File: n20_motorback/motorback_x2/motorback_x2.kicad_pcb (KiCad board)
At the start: 2 copper layers, 19.9 x 11 mm, 13 parts, among them J1 Servo wire input, J2 Conn_01x01_Male, J3 Conn_01x01_Male, J4 prog_pins, U1 DRV8837DSGR, U2 ATtiny4-TS, U3 AIC1734-33GUTR

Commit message: mechanical improvements
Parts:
- moved C1 7.83 mm to (159.2, 115.4), turned to 180 degrees
- moved C2 7.47 mm to (161.3, 115.6), turned to 90 degrees
- moved U1 7.12 mm to (164.0, 116.4), turned to 45 degrees
- moved U2 2.90 mm to (169.3, 116.6)
- moved R2 2.00 mm to (172.5, 116.8)
- moved C3 0.70 mm to (166.0, 119.7)
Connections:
- J4 pad 4: /MOTORF -> /MOTORR
- J4 pad 5: /MOTORR -> /MOTORF
- U2 pad 1: /MOTORR -> /MOTORF
- U2 pad 3: /MOTORF -> /MOTORR
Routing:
- net /MOTORF: track 23.6 -> 9.34 mm
- net VBAT: track 20.9 -> 33.1 mm, vias 0 -> 4
- net /MOTORR: track 21.5 -> 9.59 mm
- net /VLOGIC: track 32.0 -> 22.1 mm, vias 3 -> 1
- net /MOTOROUT1: track 2.90 -> 8.41 mm
- net /MOTOROUT2: track 7.38 -> 3.03 mm
- net GND: track 26.5 -> 29.8 mm, vias 8 -> 6
- net BLINKY: track 9.41 -> 11.7 mm
- net PWMIN: track 6.67 -> 8.11 mm
- net /PWMR: track 3.10 -> 2.20 mm
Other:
- outline, holes or cut-outs redrawn

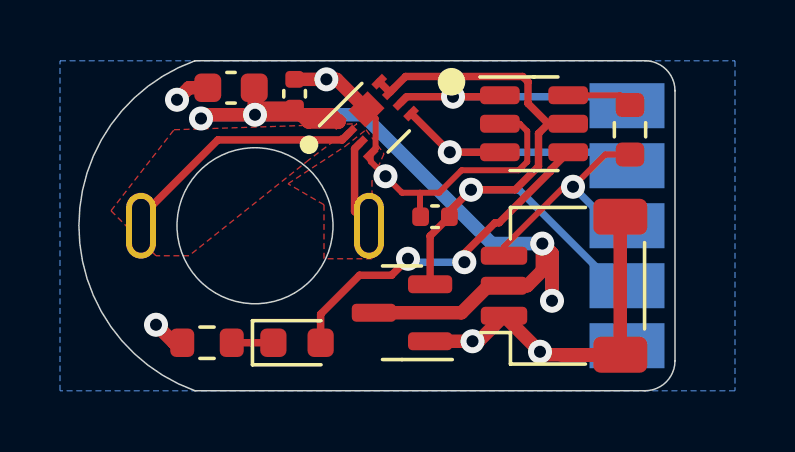
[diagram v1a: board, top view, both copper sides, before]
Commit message: Correct tpiclk / tpidata confusion
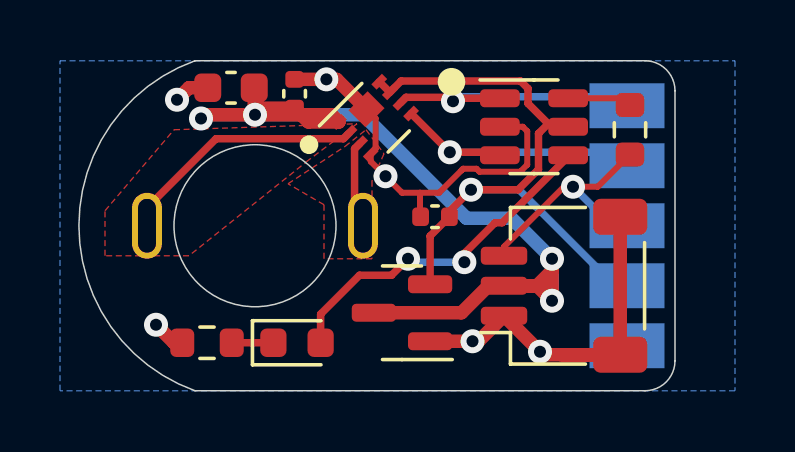
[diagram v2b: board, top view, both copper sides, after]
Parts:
- moved J2 0.20 mm to (156.6, 120.0)
- moved J3 0.20 mm to (163.4, 120.0)
- moved U2 0.10 mm to (169.3, 116.7)
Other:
- outline, holes or cut-outs redrawn

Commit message: minor fixups
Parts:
- moved U1 0.51 mm to (164.5, 116.5)
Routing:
- net /MOTOROUT1: track 8.39 -> 0.00 mm
- net /MOTOROUT2: track 2.95 -> 0.00 mm
- net /MOTORF: track 9.47 -> 8.93 mm
- net GND: track 29.9 -> 30.5 mm

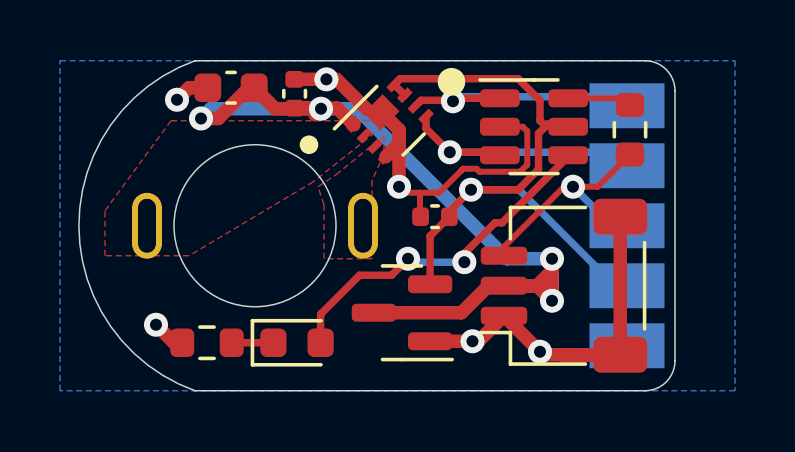
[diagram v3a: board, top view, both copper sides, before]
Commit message: Optional pull-down resistor
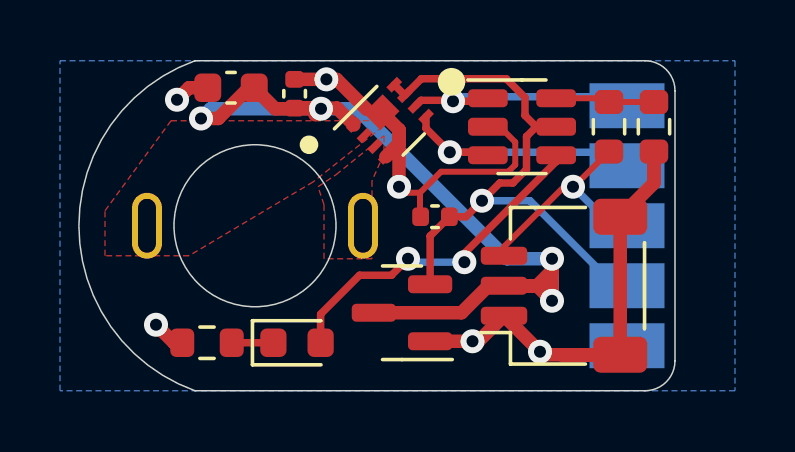
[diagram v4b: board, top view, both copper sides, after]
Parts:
- added R3: DNP, Resistor_SMD:R_0603_1608Metric, F.Cu at (173.3, 116.7)
- moved R2 0.71 mm to (171.8, 116.7)
- moved U2 0.40 mm to (168.9, 116.7)
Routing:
- net GND: track 30.5 -> 32.9 mm
- net /VLOGIC: track 21.8 -> 20.1 mm
- net /PWMR: track 2.16 -> 2.91 mm
- net PWMIN: track 8.11 -> 7.45 mm

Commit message: remove unnecessary bits
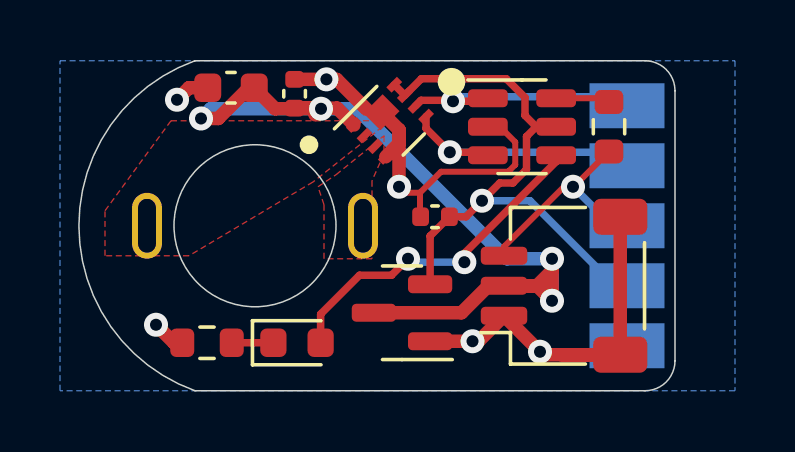
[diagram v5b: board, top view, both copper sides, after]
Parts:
- removed R3: DNP, Resistor_SMD:R_0603_1608Metric
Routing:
- net GND: track 32.9 -> 29.3 mm
- net /PWMR: track 2.91 -> 1.41 mm
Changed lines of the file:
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@@
-    )
-  )
-  (footprint "Resistor_SMD:R_0603_1608Metric" (layer "F.Cu")
-    (at 173.3 116.7 -90)
-    (descr "Resistor SMD 0603 (1608 Metric), square (rectangular) end terminal, IPC_7351 nominal, (Body size source: IPC-SM-782 page 72, https://www.pcb-3d.com/wordpress/wp-content/uploads/ipc-sm-782a_amendment_1_and_2.pdf), generated with kicad-footprint-generator")
-    (tags "resistor")
-    (property "LCSC" "")
-    (property "Sheet file" "motorback_x2.kicad_sch")
-    (property "Sheet name" "")
-    (attr smd)
-    (fp_text reference "R3" (at 0 -1.43 90) (layer "F.SilkS") hide
-      (effects (font (size 1 1) (thickness 0.15)))
-    )
-    (fp_text value "DNP" (at 0 1.43 90) (layer "F.Fab")
-      (effects (font (size 1 1) (thickness 0.15)))
-    )
-    (fp_text user "${REFERENCE}" (at 0 0 90) (layer "F.Fab")
-      (effects (font (size 0.4 0.4) (thickness 0.06)))
-    )
-    (fp_line (start -0.237258 0.5225) (end 0.237258 0.5225) (layer "F.SilkS") (width 0.12))
-    (fp_line (start -0.237258 -0.5225) (end 0.237258 -0.5225) (layer "F.SilkS") (width 0.12))
-    (fp_line (start -1.48 -0.73) (end 1.48 -0.73) (layer "F.CrtYd") (width 0.05))
-    (fp_line (start -1.48 0.73) (end -1.48 -0.73) (layer "F.CrtYd") (width 0.05))
-    (fp_line (start 1.48 0.73) (end -1.48 0.73) (layer "F.CrtYd") (width 0.05))
-    (fp_line (start 1.48 -0.73) (end 1.48 0.73) (layer "F.CrtYd") (width 0.05))
-    (fp_line (start -0.8 -0.4125) (end 0.8 -0.4125) (layer "F.Fab") (width 0.1))
-    (fp_line (start -0.8 0.4125) (end -0.8 -0.4125) (layer "F.Fab") (width 0.1))
-    (fp_line (start 0.8 0.4125) (end -0.8 0.4125) (layer "F.Fab") (width 0.1))
-    (fp_line (start 0.8 -0.4125) (end 0.8 0.4125) (layer "F.Fab") (width 0.1))
-    (pad "1" smd roundrect (at -0.825 0 270) (locked) (size 0.8 0.95) (layers "F.Cu" "F.Paste" "F.Mask") (roundrect_rratio 0.25)
-      (net 11 "/PWMR"))
-    (pad "2" smd roundrect (at 0.825 0 270) (locked) (size 0.8 0.95) (layers "F.Cu" "F.Paste" "F.Mask") (roundrect_rratio 0.25)
-      (net 1 "GND"))
-    (model "${KICAD6_3DMODEL_DIR}/Resistor_SMD.3dshapes/R_0603_1608Metric.wrl"
-      (offset (xyz 0 0 0))
-      (scale (xyz 1 1 1))
-      (rotate (xyz 0 0 0))
     )
   )
@@
   (segment (start 157.575 123.9) (end 157.3 123.9) (width 0.45) (layer "F.Cu") (net 1))
   (segment (start 168.1625 116.7) (end 168.67502 117.21252) (width 0.2) (layer "F.Cu") (net 1))
-  (segment (start 173.3 118.575) (end 173.3 117.525) (width 0.45) (layer "F.Cu") (net 1))
   (segment (start 164.8 116.8) (end 164.8 117.260661) (width 0.45) (layer "F.Cu") (net 1))
   (segment (start 170.2 124.3) (end 172.175 124.3) (width 0.45) (layer "F.Cu") (net 1))
   (segment (start 166.19998 118.20002) (end 165.5 118.9) (width 0.2) (layer "F.Cu") (net 1))
   (segment (start 162.72 115.12) (end 163.717157 116.117157) (width 0.45) (layer "F.Cu") (net 1))
-  (segment (start 172.175 119.7) (end 173.3 118.575) (width 0.45) (layer "F.Cu") (net 1))
   (segment (start 172.175 119.7) (end 172.175 124.3) (width 0.45) (layer "F.Cu") (net 1))
-  (segment (start 173.3 118.5) (end 173.3 117.525) (width 0.45) (layer "F.Cu") (net 1))
   (segment (start 162.38 115.12) (end 162.72 115.12) (width 0.45) (layer "F.Cu") (net 1))
   (segment (start 164.8 117.260661) (end 164.358579 117.702082) (width 0.45) (layer "F.Cu") (net 1))
@@
   (segment (start 166.978767 121.214263) (end 165.214263 121.214263) (width 0.25) (layer "B.Cu") (net 7))
   (segment (start 159.225 123.9) (end 160.6125 123.9) (width 0.25) (layer "F.Cu") (net 8))
-  (segment (start 171.8 115.875) (end 173.3 115.875) (width 0.2) (layer "F.Cu") (net 11))
   (segment (start 171.675 115.75) (end 171.8 115.875) (width 0.2) (layer "F.Cu") (net 11))
   (segment (start 170.4375 115.75) (end 171.675 115.75) (width 0.2) (layer "F.Cu") (net 11))

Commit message: Use 1k resistors
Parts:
- R1, R2: value 680R -> 1k

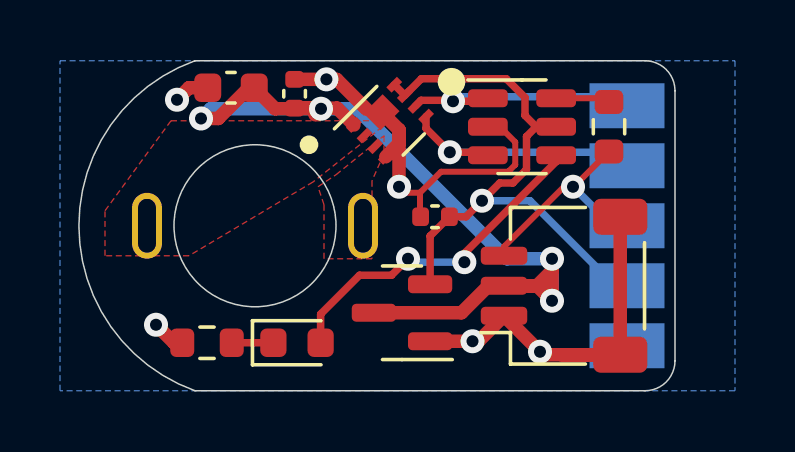
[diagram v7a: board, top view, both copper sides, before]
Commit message: Slighty bigger motor holes; slightly smaller vias
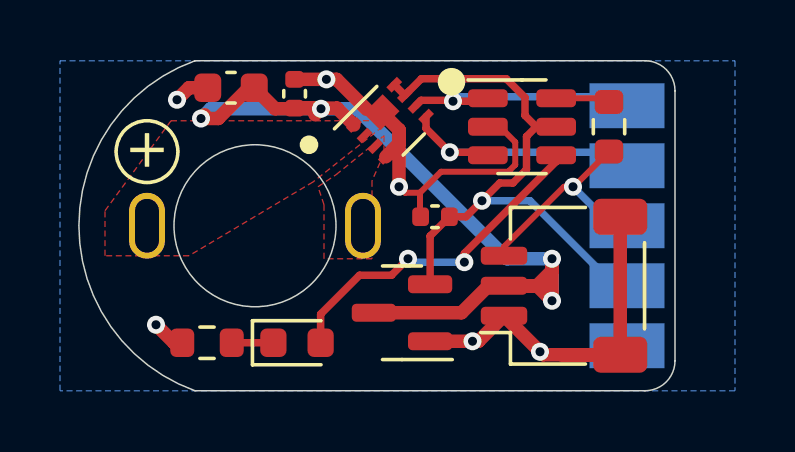
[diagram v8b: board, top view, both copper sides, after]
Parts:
- moved J2 0.20 mm to (156.4, 120.0)
- moved J3 0.20 mm to (163.6, 120.0)
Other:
- board text added: "+"
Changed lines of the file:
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@@
-(kicad_pcb (version 20210126) (generator pcbnew)
+(kicad_pcb (version 20210228) (generator pcbnew)
   (general
     (thickness 0.89)
@@
       (dielectric_constraints no)
     )
+    (pad_to_mask_clearance 0)
     (aux_axis_origin 160 120)
     (pcbplotparams
@@
     (pad "3" smd roundrect (at 1 -2 90) (locked) (size 0.6 1.55) (layers "F.Cu" "F.Paste" "F.Mask") (roundrect_rratio 0.25)
       (net 4 "PWMIN") (pinfunction "Pin_3") (pintype "passive"))
-    (pad "MP" smd roundrect (at -2.3 1.875 90) (locked) (size 1.2 1.8) (layers "F.Cu" "F.Paste" "F.Mask") (roundrect_rratio 0.208333)
+    (pad "MP" smd roundrect (at -2.3 1.875 90) (locked) (size 1.2 1.8) (layers "F.Cu" "F.Paste" "F.Mask") (roundrect_rratio 0.2083333333333333)
       (net 1 "GND") (pinfunction "MP") (pintype "passive"))
-    (pad "MP" smd roundrect (at 2.3 1.875 90) (locked) (size 1.2 1.8) (layers "F.Cu" "F.Paste" "F.Mask") (roundrect_rratio 0.208333)
+    (pad "MP" smd roundrect (at 2.3 1.875 90) (locked) (size 1.2 1.8) (layers "F.Cu" "F.Paste" "F.Mask") (roundrect_rratio 0.2083333333333333)
       (net 1 "GND") (pinfunction "MP") (pintype "passive"))
     (model "${KICAD6_3DMODEL_DIR}/Connector_JST.3dshapes/JST_SH_SM03B-SRSS-TB_1x03-1MP_P1.00mm_Horizontal.wrl"
@@
   )
   (footprint "motorback:motorpad" (layer "F.Cu")
-    (at 163.4 120)
+    (at 163.6 120)
     (property "Sheetfile" "motorback_x2.kicad_sch")
     (property "Sheetname" "")
@@
       (effects (font (size 1 1) (thickness 0.15)))
     )
-    (pad "1" thru_hole oval (at 0.2 0) (size 1 2.2) (drill oval 0.6 1.8) (layers *.Cu *.Mask)
-      (net 10 "/MOTOROUT2") (pinfunction "Pin_1") (pintype "passive"))
+    (pad "1" thru_hole oval (at 0 0) (size 1.2 2.2) (drill oval 0.8 1.8) (layers *.Cu *.Mask)
+      (net 10 "/MOTOROUT2") (pinfunction "Pin_1"))
   )
   (footprint "Package_TO_SOT_SMD:SOT-23-6" (layer "F.Cu")
@@
   )
   (footprint "motorback:motorpad" (layer "F.Cu")
-    (at 156.6 120)
+    (at 156.4 120)
     (property "Sheetfile" "motorback_x2.kicad_sch")
     (property "Sheetname" "")
@@
       (effects (font (size 1 1) (thickness 0.15)))
     )
-    (pad "1" thru_hole oval (at -0.2 0) (size 1 2.2) (drill oval 0.6 1.8) (layers *.Cu *.Mask)
-      (net 9 "/MOTOROUT1") (pinfunction "Pin_1") (pintype "passive"))
+    (pad "1" thru_hole oval (at 0 0) (size 1.2 2.2) (drill oval 0.8 1.8) (layers *.Cu *.Mask)
+      (net 9 "/MOTOROUT1") (pinfunction "Pin_1"))
   )
   (footprint "LED_SMD:LED_0603_1608Metric" (layer "F.Cu")
@@
       (net 5 "/MOTORF") (pinfunction "Pin_5") (pintype "passive"))
   )
+  (gr_circle (center 156.4 117.529563) (end 157.3 117.029563) (layer "F.SilkS") (width 0.12) (fill none))
   (gr_circle (center 166.55 115.2) (end 166.95 115.2) (layer "F.SilkS") (width 0.12) (fill solid))
   (gr_circle (center 161.8 117.3) (end 162.05 117.3) (layer "F.SilkS") (width 0.12) (fill solid))
@@
   (gr_arc (start 173 124.5) (end 173 125.5) (angle -90) (layer "Edge.Cuts") (width 0.05))
   (gr_line (start 158 125.5) (end 173 125.5) (layer "Edge.Cuts") (width 0.05))
-  (gr_text "@markxr\n2021" (at 168.6 122 270) (layer "B.SilkS")
-    (effects (font (size 1 1) (thickness 0.15)) (justify mirror))
+  (gr_text "@markxr\n2021" (at 168.4 118.6 270) (layer "B.SilkS")
+    (effects (font (size 1.2 1.2) (thickness 0.15)) (justify mirror))
+  )
+  (gr_text "+" (at 156.4 117.429563) (layer "F.SilkS")
+    (effects (font (size 1.3 1.3) (thickness 0.15)))
   )
   (gr_text "TPICLK" (at 177.5 118) (layer "Dwgs.User")
@@
   (segment (start 169.6 124.3) (end 172.175 124.3) (width 0.45) (layer "F.Cu") (net 1))
   (segment (start 158.425 115.4) (end 157.8 115.4) (width 0.45) (layer "F.Cu") (net 1))
-  (via (at 156.7 123.3) (size 0.8) (drill 0.4) (layers "F.Cu" "B.Cu") (net 1))
-  (via (at 162.38 115.12) (size 0.8) (drill 0.4) (layers "F.Cu" "B.Cu") (net 1))
-  (via (at 169.5 124.2) (size 0.8) (drill 0.4) (layers "F.Cu" "B.Cu") (net 1))
-  (via (at 167.25 123.85) (size 0.8) (drill 0.4) (layers "F.Cu" "B.Cu") (net 1))
-  (via (at 157.4 115.8) (size 0.8) (drill 0.4) (layers "F.Cu" "B.Cu") (net 1))
-  (via (at 164.8 118.7) (size 0.8) (drill 0.4) (layers "F.Cu" "B.Cu") (net 1))
+  (via (at 156.7 123.3) (size 0.6) (drill 0.3) (layers "F.Cu" "B.Cu") (net 1))
+  (via (at 162.38 115.12) (size 0.6) (drill 0.3) (layers "F.Cu" "B.Cu") (net 1))
+  (via (at 169.5 124.2) (size 0.6) (drill 0.3) (layers "F.Cu" "B.Cu") (net 1))
+  (via (at 167.25 123.85) (size 0.6) (drill 0.3) (layers "F.Cu" "B.Cu") (net 1))
+  (via (at 157.4 115.8) (size 0.6) (drill 0.3) (layers "F.Cu" "B.Cu") (net 1))
+  (via (at 164.8 118.7) (size 0.6) (drill 0.3) (layers "F.Cu" "B.Cu") (net 1))
   (segment (start 169.9 121.175) (end 169.9 121.1) (width 0.45) (layer "F.Cu") (net 2))
   (segment (start 169.4 122) (end 169.075 122) (width 0.45) (layer "F.Cu") (net 2))
@@
   (segment (start 161.32 116.08) (end 162.18 116.08) (width 0.45) (layer "F.Cu") (net 2))
   (segment (start 160.675 116.1) (end 162.2 116.1) (width 0.45) (layer "F.Cu") (net 2))
-  (via (at 169.9 122.5) (size 0.8) (drill 0.4) (layers "F.Cu" "B.Cu") (net 2))
-  (via (at 158.20018 116.425012) (size 0.8) (drill 0.4) (layers "F.Cu" "B.Cu") (net 2))
-  (via (at 162.2 116.1) (size 0.8) (drill 0.4) (layers "F.Cu" "B.Cu") (net 2))
-  (via (at 169.9 121.1) (size 0.8) (drill 0.4) (layers "F.Cu" "B.Cu") (net 2))
+  (via (at 169.9 122.5) (size 0.6) (drill 0.3) (layers "F.Cu" "B.Cu") (net 2))
+  (via (at 158.20018 116.425012) (size 0.6) (drill 0.3) (layers "F.Cu" "B.Cu") (net 2))
+  (via (at 162.2 116.1) (size 0.6) (drill 0.3) (layers "F.Cu" "B.Cu") (net 2))
+  (via (at 169.9 121.1) (size 0.6) (drill 0.3) (layers "F.Cu" "B.Cu") (net 2))
   (segment (start 158.20018 116.425012) (end 158.525192 116.1) (width 0.45) (layer "B.Cu") (net 2))
   (segment (start 169.9 121.1) (end 168.4 121.1) (width 0.45) (layer "B.Cu") (net 2))
@@
   (segment (start 165.546447 115.1) (end 166.7 115.1) (width 0.25) (layer "F.Cu") (net 3))
   (segment (start 166.48 119.7) (end 165.8375 120.3425) (width 0.25) (layer "F.Cu") (net 3))
-  (via (at 167.566445 119.166445) (size 0.8) (drill 0.4) (layers "F.Cu" "B.Cu") (net 3))
+  (via (at 167.566445 119.166445) (size 0.6) (drill 0.3) (layers "F.Cu" "B.Cu") (net 3))
   (segment (start 169.166445 119.166445) (end 167.566445 119.166445) (width 0.25) (layer "B.Cu") (net 3))
   (segment (start 172 122) (end 169.166445 119.166445) (width 0.25) (layer "B.Cu") (net 3))
@@
   (segment (start 168.3 121) (end 168.3 120.7) (width 0.2) (layer "F.Cu") (net 4))
   (segment (start 170.625 118.7) (end 171.8 117.525) (width 0.2) (layer "F.Cu") (net 4))
-  (via (at 170.6 118.7) (size 0.8) (drill 0.4) (layers "F.Cu" "B.Cu") (net 4))
+  (via (at 170.6 118.7) (size 0.6) (drill 0.3) (layers "F.Cu" "B.Cu") (net 4))
   (segment (start 172.4 120) (end 171.9 120) (width 0.25) (layer "B.Cu") (net 4))
   (segment (start 171.9 120) (end 170.6 118.7) (width 0.25) (layer "B.Cu") (net 4))
@@
   (segment (start 167.66251 115.84999) (end 167.7625 115.75) (width 0.25) (layer "F.Cu") (net 5))
   (segment (start 166.568404 115.818394) (end 165.535159 115.818394) (width 0.25) (layer "F.Cu") (net 5))
-  (via (at 166.6 115.84999) (size 0.8) (drill 0.4) (layers "F.Cu" "B.Cu") (net 5))
+  (via (at 166.6 115.84999) (size 0.6) (drill 0.3) (layers "F.Cu" "B.Cu") (net 5))
   (segment (start 172.1 115.7) (end 166.74999 115.7) (width 0.25) (layer "B.Cu") (net 5))
   (segment (start 172.4 116) (end 172.1 115.7) (width 0.25) (layer "B.Cu") (net 5))
@@
   (segment (start 167.6625 117.55) (end 167.7625 117.65) (width 0.25) (layer "F.Cu") (net 6))
   (segment (start 166.493503 117.55) (end 167.6625 117.55) (width 0.25) (layer "F.Cu") (net 6))
-  (via (at 166.493503 117.55) (size 0.8) (drill 0.4) (layers "F.Cu" "B.Cu") (net 6))
+  (via (at 166.493503 117.55) (size 0.6) (drill 0.3) (layers "F.Cu" "B.Cu") (net 6))
   (segment (start 166.493503 117.55) (end 171.95 117.55) (width 0.25) (layer "B.Cu") (net 6))
   (segment (start 171.95 117.55) (end 172.4 118) (width 0.25) (layer "B.Cu") (net 6))
@@
   (segment (start 164.54998 121.65002) (end 165.1 121.1) (width 0.25) (layer "F.Cu") (net 7))
   (segment (start 163.485002 121.65002) (end 164.54998 121.65002) (width 0.25) (layer "F.Cu") (net 7))
-  (via (at 166.978767 121.214263) (size 0.8) (drill 0.4) (layers "F.Cu" "B.Cu") (net 7))
-  (via (at 165.1 121.1) (size 0.8) (drill 0.4) (layers "F.Cu" "B.Cu") (net 7))
+  (via (at 166.978767 121.214263) (size 0.6) (drill 0.3) (layers "F.Cu" "B.Cu") (net 7))
+  (via (at 165.1 121.1) (size 0.6) (drill 0.3) (layers "F.Cu" "B.Cu") (net 7))
   (segment (start 165.214263 121.214263) (end 165.1 121.1) (width 0.25) (layer "B.Cu") (net 7))
   (segment (start 166.978767 121.214263) (end 165.214263 121.214263) (width 0.25) (layer "B.Cu") (net 7))
